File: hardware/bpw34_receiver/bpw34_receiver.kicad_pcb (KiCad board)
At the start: 2 copper layers, 70 x 32 mm, 25 parts, among them J1 A2 / RED, J2 A0 / IR, J3 ADS1115: RED/GND/IR/GND, U1 OPA333AIDBVR, U2 OPA333AIDBVR

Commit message: hardware: clarify BPW34 schematic and route supplies clear of mounting holes
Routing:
- net /3V3_RED: track 65.3 -> 67.7 mm
- net /3V3_IR: track 74.3 -> 76.7 mm
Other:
- board text added: "PPG BPW34 RX v1.2"
- board text removed: "PPG BPW34 RX v1.1"

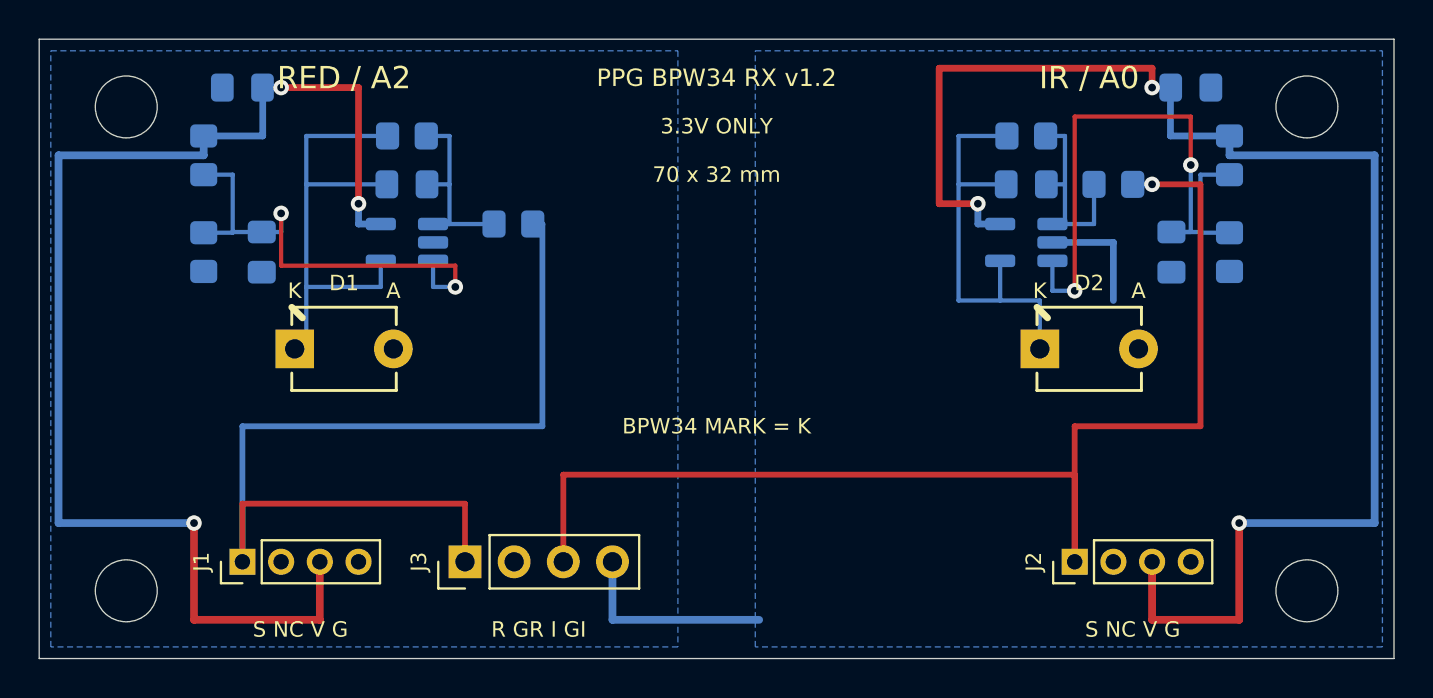
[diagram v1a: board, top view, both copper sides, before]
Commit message: Compact PPG boards, add receiver filters and package V-cut panel
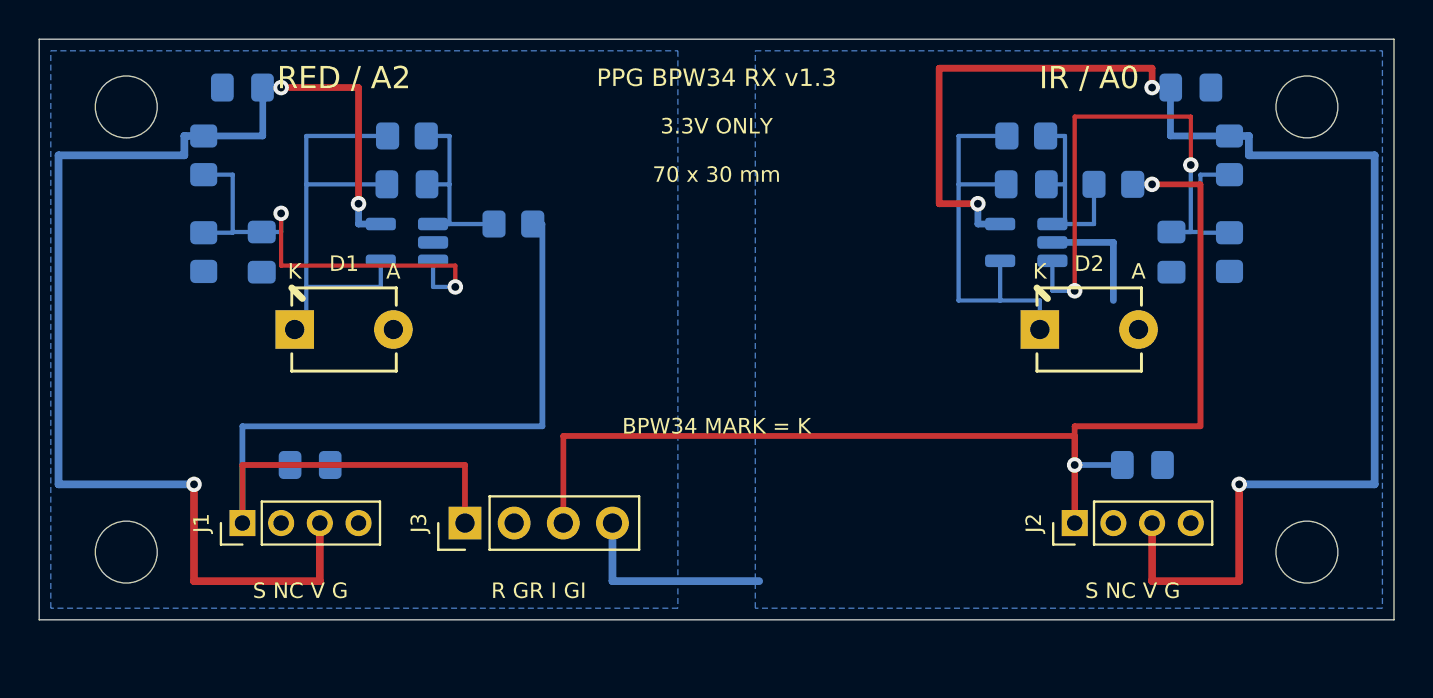
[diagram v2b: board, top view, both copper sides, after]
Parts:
- added C7: 1uF X7R 16V, PPG:C0805_Hand, B.Cu at (114.0, 122.0)
- added C8: 1uF X7R 16V, PPG:C0805_Hand, B.Cu at (157.0, 122.0)
- R3, R4: value 100R -> 1k 1%
- moved H3 2.00 mm to (104.5, 126.5)
- moved H4 2.00 mm to (165.5, 126.5)
- moved J1 2.00 mm to (110.5, 125.0)
- moved J2 2.00 mm to (153.5, 125.0)
- moved J3 2.00 mm to (122.0, 125.0)
- moved D1 1.00 mm to (115.8, 115.0)
- moved D2 1.00 mm to (154.2, 115.0)
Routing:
- net /3V3_RED: track 67.7 -> 65.7 mm
- net /3V3_IR: track 76.7 -> 74.7 mm
- net /SUM_IR: track 22.2 -> 21.2 mm
- net /OUT_IR: track 64.9 -> 65.4 mm, vias 1 -> 2
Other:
- board size 70 x 32 mm -> 70 x 30 mm
- board text added: "70 x 30 mm"
- board text added: "PPG BPW34 RX v1.3"
- board text removed: "70 x 32 mm"
- board text removed: "PPG BPW34 RX v1.2"

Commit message: Shrink PPG receivers to 70x20 and driver to 70x40; refresh V-cut release
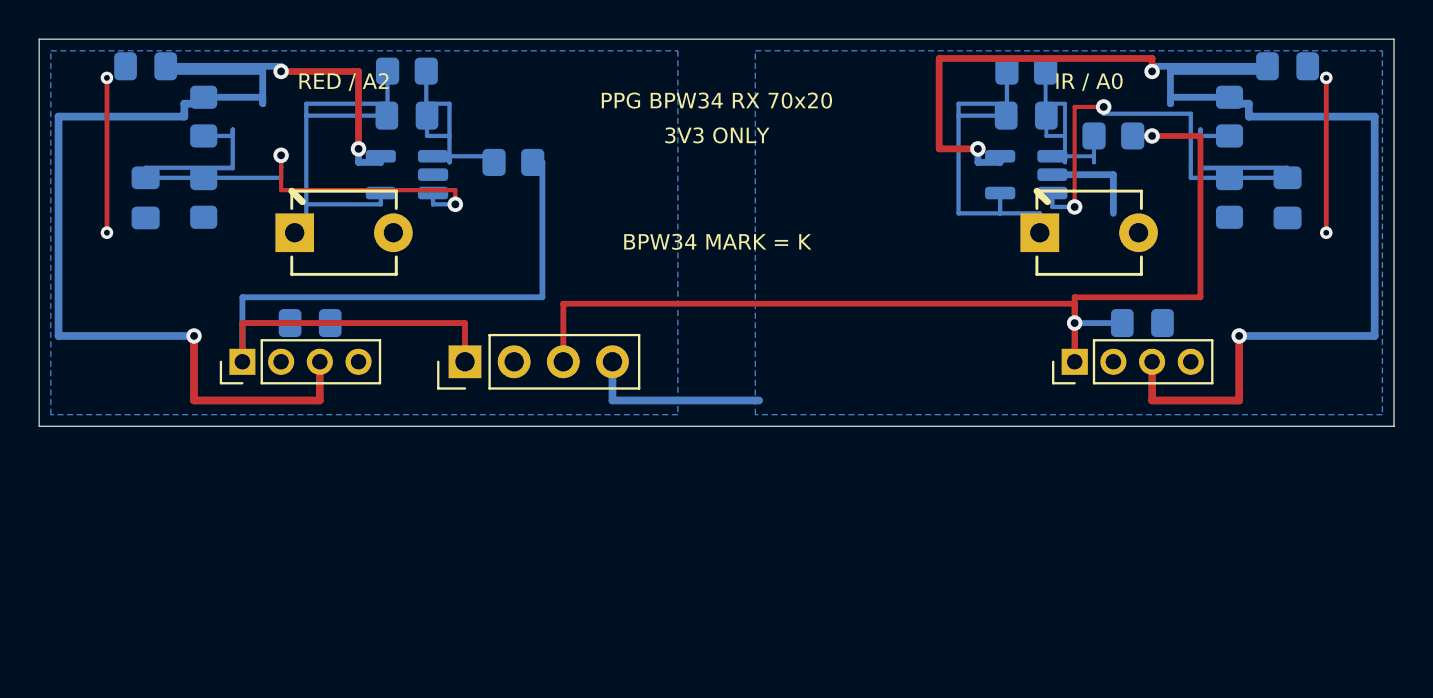
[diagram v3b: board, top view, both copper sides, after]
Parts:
- removed H1, H2, H3, H4: M3 / 3.2mm NPTH, PPG:MountingHole_M3
- moved J1 8.33 mm to (110.5, 116.7)
- moved J2 8.33 mm to (153.5, 116.7)
- moved J3 8.33 mm to (122.0, 116.7)
- moved C7 7.33 mm to (114.0, 114.7)
- moved C8 7.33 mm to (157.0, 114.7)
- moved C3 6.62 mm to (105.5, 108.2)
- moved C4 6.62 mm to (164.5, 108.2)
- moved C5 5.12 mm to (105.5, 101.4)
- moved C6 5.12 mm to (164.5, 101.4)
- moved D1 5.00 mm to (115.8, 110.0)
- moved D2 5.00 mm to (154.2, 110.0)
- moved C1 3.55 mm to (119.0, 104.0)
- moved C2 3.55 mm to (151.0, 104.0)
- moved U1 3.50 mm to (119.0, 107.0)
- moved U2 3.50 mm to (151.0, 107.0)
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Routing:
- net /OUT_IR: track 65.4 -> 56.5 mm
- net /GND_RED: track 0.00 -> 8.00 mm, vias 0 -> 2
- net /VREF_RED: track 24.8 -> 32.3 mm
- net /OUT_RED: track 51.4 -> 44.3 mm
- net /GND_IR: track 16.7 -> 22.7 mm, vias 0 -> 2
- net /SUM_RED: track 25.0 -> 22.3 mm
- net /SUM_IR: track 21.2 -> 18.6 mm
- net /FB_RED: track 10.9 -> 12.8 mm
- net /FB_IR: track 11.4 -> 12.5 mm
- net /3V3_IR: track 74.7 -> 73.7 mm
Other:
- board size 70 x 30 mm -> 70 x 20 mm
- board text added: "3V3 ONLY"
- board text added: "NC"
- board text added: "PPG BPW34 RX 70x20"
- board text removed: "3.3V ONLY"
- board text removed: "70 x 30 mm"
- board text removed: "D1 RED"
- board text removed: "D2 IR"
- board text removed: "GR/GI=CHANNEL GND"
- board text removed: "J1 A2 RED"
- board text removed: "J2 A0 IR"
- board text removed: "J3 ADS"
- board text removed: "N"
- board text removed: "PPG BPW34 RX v1.3"
- board text removed: "R GR I GI"
- board text removed: "R=OUT_RED I=OUT_IR"
- board text removed: "S NC V G"
- board text removed: "V=3V3 N=NC"

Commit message: Increase V-score copper and component margins; reposition receiver circuits
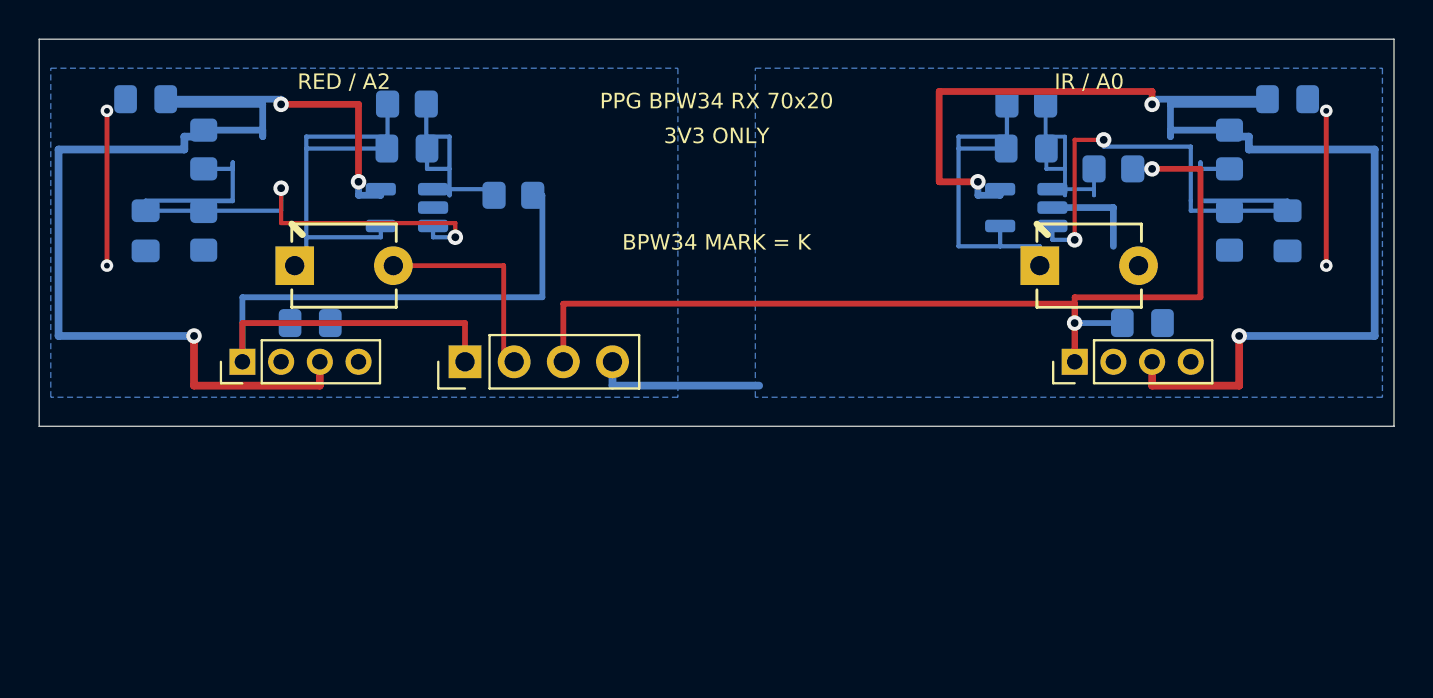
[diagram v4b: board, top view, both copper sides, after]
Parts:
- moved C1 1.70 mm to (119.0, 105.7)
- moved C2 1.70 mm to (151.0, 105.7)
- moved C3 1.70 mm to (105.5, 109.9)
- moved C4 1.70 mm to (164.5, 109.9)
- moved D1 1.70 mm to (115.8, 111.7)
- moved D2 1.70 mm to (154.2, 111.7)
- moved R3 1.70 mm to (124.5, 108.1)
- moved R4 1.70 mm to (155.5, 106.7)
- moved R5 1.70 mm to (108.5, 105.7)
- moved R6 1.70 mm to (161.5, 105.7)
- moved R7 1.70 mm to (108.5, 109.9)
- moved R8 1.70 mm to (161.5, 109.9)
- moved U1 1.70 mm to (119.0, 108.7)
- moved U2 1.70 mm to (151.0, 108.7)
- moved C5 1.70 mm to (105.5, 103.1)
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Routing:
- net /GND_RED: track 8.00 -> 19.2 mm
- net /3V3_IR: track 73.7 -> 70.5 mm
- net /3V3_RED: track 65.4 -> 62.2 mm
- net /OUT_RED: track 44.3 -> 42.6 mm
- net /OUT_IR: track 56.5 -> 54.8 mm
- net /GND_IR: track 22.7 -> 22.0 mm

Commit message: Chamfer PPG board routing to 45 degrees and verify V-score fabrication release
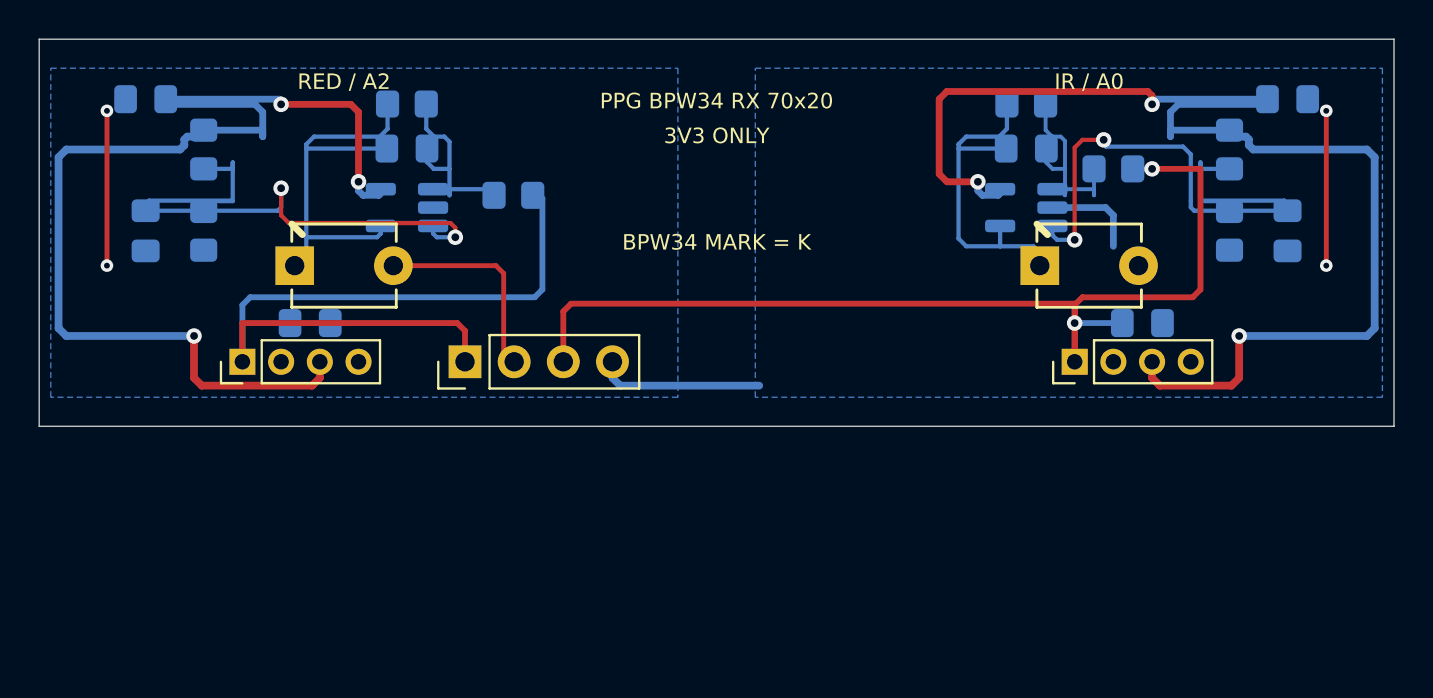
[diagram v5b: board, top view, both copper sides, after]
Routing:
- net /3V3_IR: track 70.5 -> 68.1 mm
- net /3V3_RED: track 62.2 -> 60.2 mm
- net /SUM_IR: track 18.6 -> 17.7 mm
- net /VREF_IR: track 32.6 -> 31.7 mm
- net /OUT_RED: track 42.6 -> 41.8 mm
- net /SUM_RED: track 22.3 -> 21.5 mm
- net /OUT_IR: track 54.8 -> 54.1 mm
- net /VREF_RED: track 32.3 -> 31.6 mm
- net /FB_RED: track 12.8 -> 12.1 mm
- net /FB_IR: track 12.5 -> 12.0 mm

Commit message: Lengthen 45-degree PCB bends and refresh fabrication packages
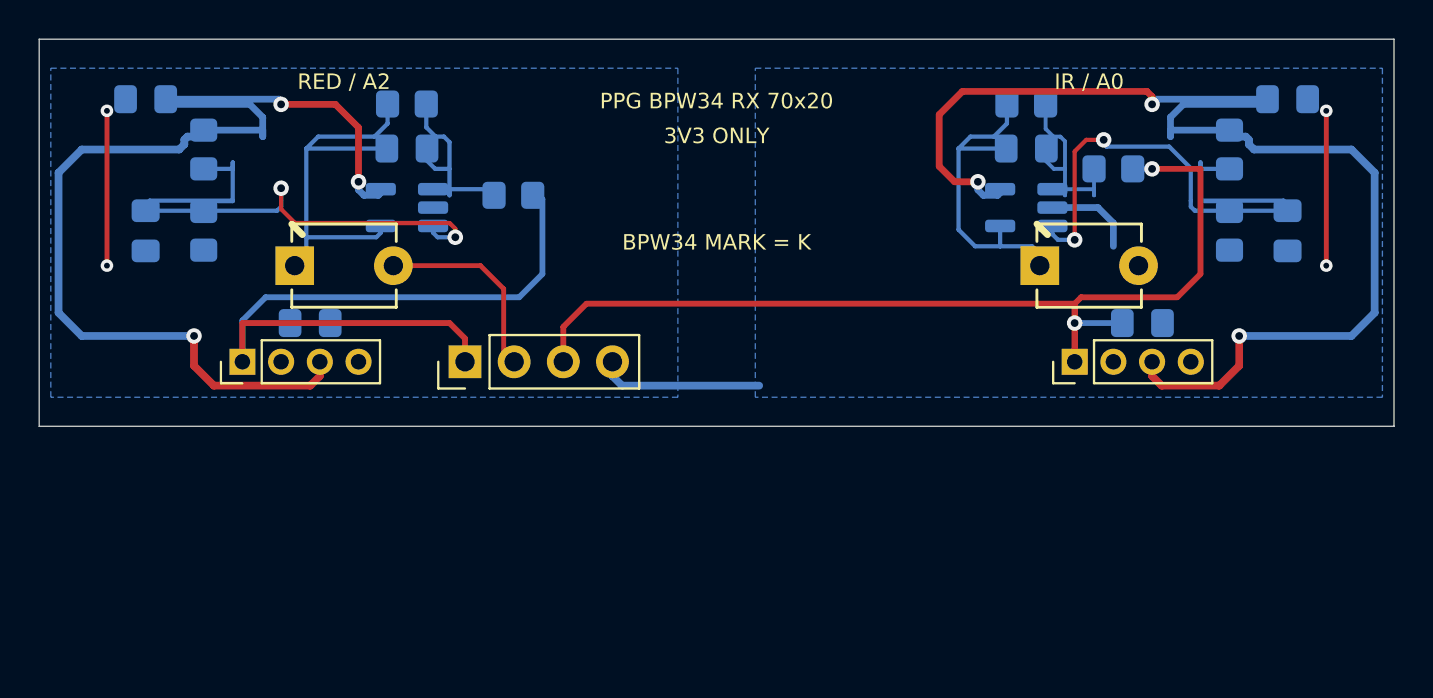
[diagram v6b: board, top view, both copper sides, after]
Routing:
- net /3V3_IR: track 68.1 -> 65.8 mm
- net /3V3_RED: track 60.2 -> 58.1 mm
- net /OUT_RED: track 41.8 -> 40.6 mm
- net /OUT_IR: track 54.1 -> 53.2 mm
- net /VREF_IR: track 31.7 -> 31.1 mm
- net /SUM_IR: track 17.7 -> 17.1 mm

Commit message: Update README.md, hardware 45-degree routing and OPT101 diagnostic docs
- Fix version line in README.md to ensure version consistency test passes
- Document persistent live A0/A2 RX monitor dock and touch UI scaling
- Document OPT101 physical bench diagnostic protocol (docs/opt101-a0-diagnostic-2026-10-01.md)
- Detail 45-degree chamfered PCB routing, segment cleanup, and updated wiring guides
- Update repository tree and refreshed manufacturing release ZIPs
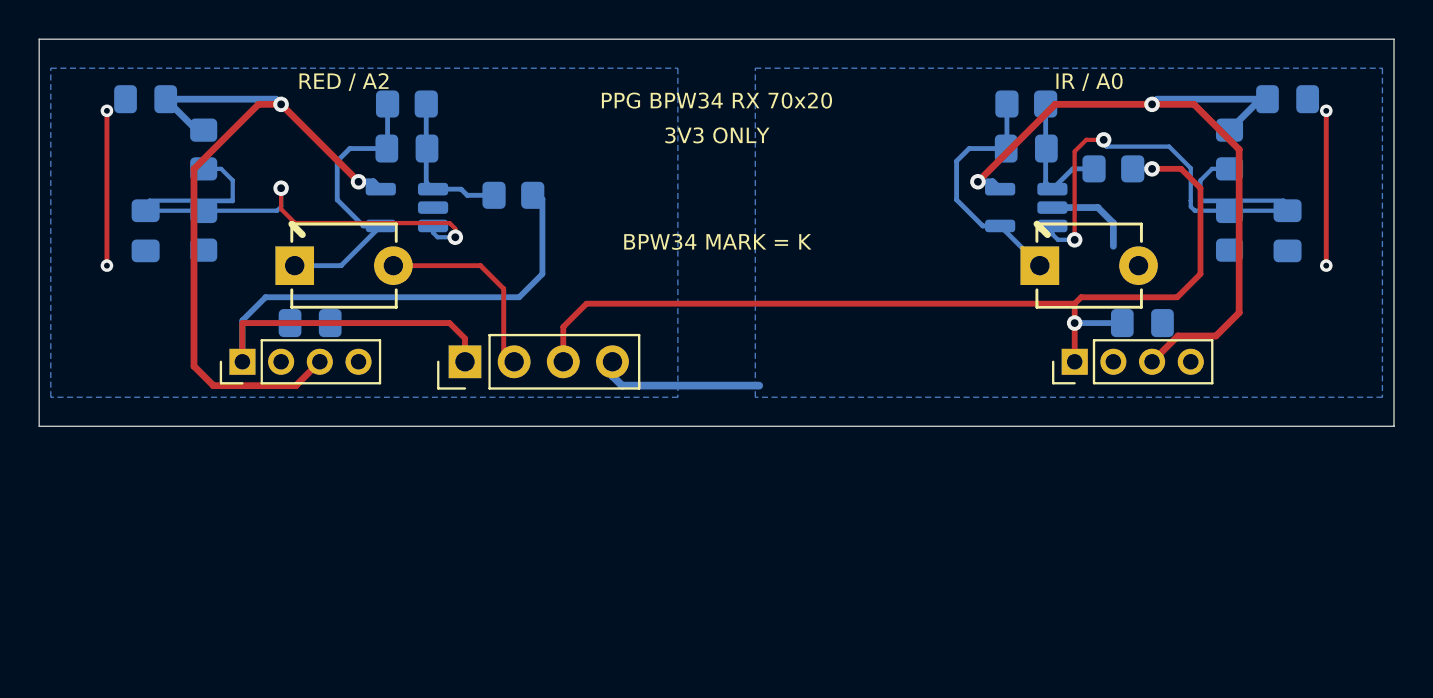
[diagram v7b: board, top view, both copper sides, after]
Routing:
- net /3V3_IR: track 65.8 -> 39.8 mm, vias 3 -> 2
- net /3V3_RED: track 58.1 -> 39.2 mm, vias 3 -> 2
- net /SUM_RED: track 21.2 -> 15.2 mm
- net /FB_IR: track 11.9 -> 7.13 mm
- net /SUM_IR: track 17.1 -> 12.8 mm
- net /FB_RED: track 12.0 -> 7.83 mm
- net /OUT_IR: track 53.2 -> 49.7 mm
- net /VREF_IR: track 31.1 -> 30.1 mm
- net /VREF_RED: track 31.3 -> 30.3 mm
